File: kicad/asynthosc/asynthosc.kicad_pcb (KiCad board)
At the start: 4 copper layers, 69 x 106 mm, 210 parts, among them J1 USB_B_Micro, J10 AudioJack3, J11 AudioJack3, J12 RJ45_LED_Shielded, J13 AudioJack3, J14 AudioJack3, J2 Conn_02x05_Odd_Even, J3 Conn_ARM_SWD_TagConnect_TC203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, J4 Conn_02x07_Odd_Even, J5 Conn_02x04_Odd_Even, J6 AudioJack3, J7 AudioJack3, J8 AudioJack3, J9 AudioJack3, Q1 Q_NPN_BEC, Q2 Q_NPN_BEC, SW1 SW_Push, SW2 SW_MEC_5G_LED, SW3 SW_DIP_x02, SW4 SW_DIP_x02, SW5 SW_MEC_5G_LED, SW6 RotaryEncoder, SW7 SW_MEC_5G_LED, SW8 SW_MEC_5G_LED, U1 LM1117S-3.3, U10 LAN8742A, U11 USBLC6-2P6, U12 H11L1, U13 USBLC6-2P6, U2 LMR62421XMF, U3 USBLC6-2SC6, U4 LM1117S-5.0, U5 Si1869DH, U6 STM32F723VETx, U7 W25Q32JVSS, U8 MCP6004, U9 MCP6004, Y1 8MHz, 8pF, Y2 25MHZ,20PF,30PPM

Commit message: pcb: routing
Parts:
- moved SW1 5.54 mm to (101.8, 108.2)
- moved D22 4.98 mm to (89.8, 111.8)
- moved R69 0.50 mm to (130.8, 124.8)
- turned R32 to 0 degrees
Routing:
- net 5V: track 160.1 -> 141.3 mm
- net GND: track 42.5 -> 57.5 mm, vias 214 -> 316
- net /Soc/NRST: track 31.6 -> 39.5 mm
- net Net-(U8A--): track 0.00 -> 7.10 mm
- net /Soc/JTCK_CONN: track 61.7 -> 56.5 mm
- net /Analog_in/CVIN1: track 69.1 -> 65.0 mm
- net Net-(SW3B-2): track 1.49 -> 3.69 mm
- net Net-(SW3A-2): track 0.00 -> 2.19 mm
- net Net-(J6-PadT): track 37.4 -> 39.3 mm
- net 3V3_FILT: track 9.46 -> 8.76 mm, vias 9 -> 11
- net /Soc/Ethernet/TX_P: track 25.3 -> 24.7 mm
- net /Soc/Ethernet/TX_N: track 26.6 -> 26.0 mm
- net /Analog_in/CVIN0: track 70.5 -> 71.0 mm
- net 3V3: vias 19 -> 48

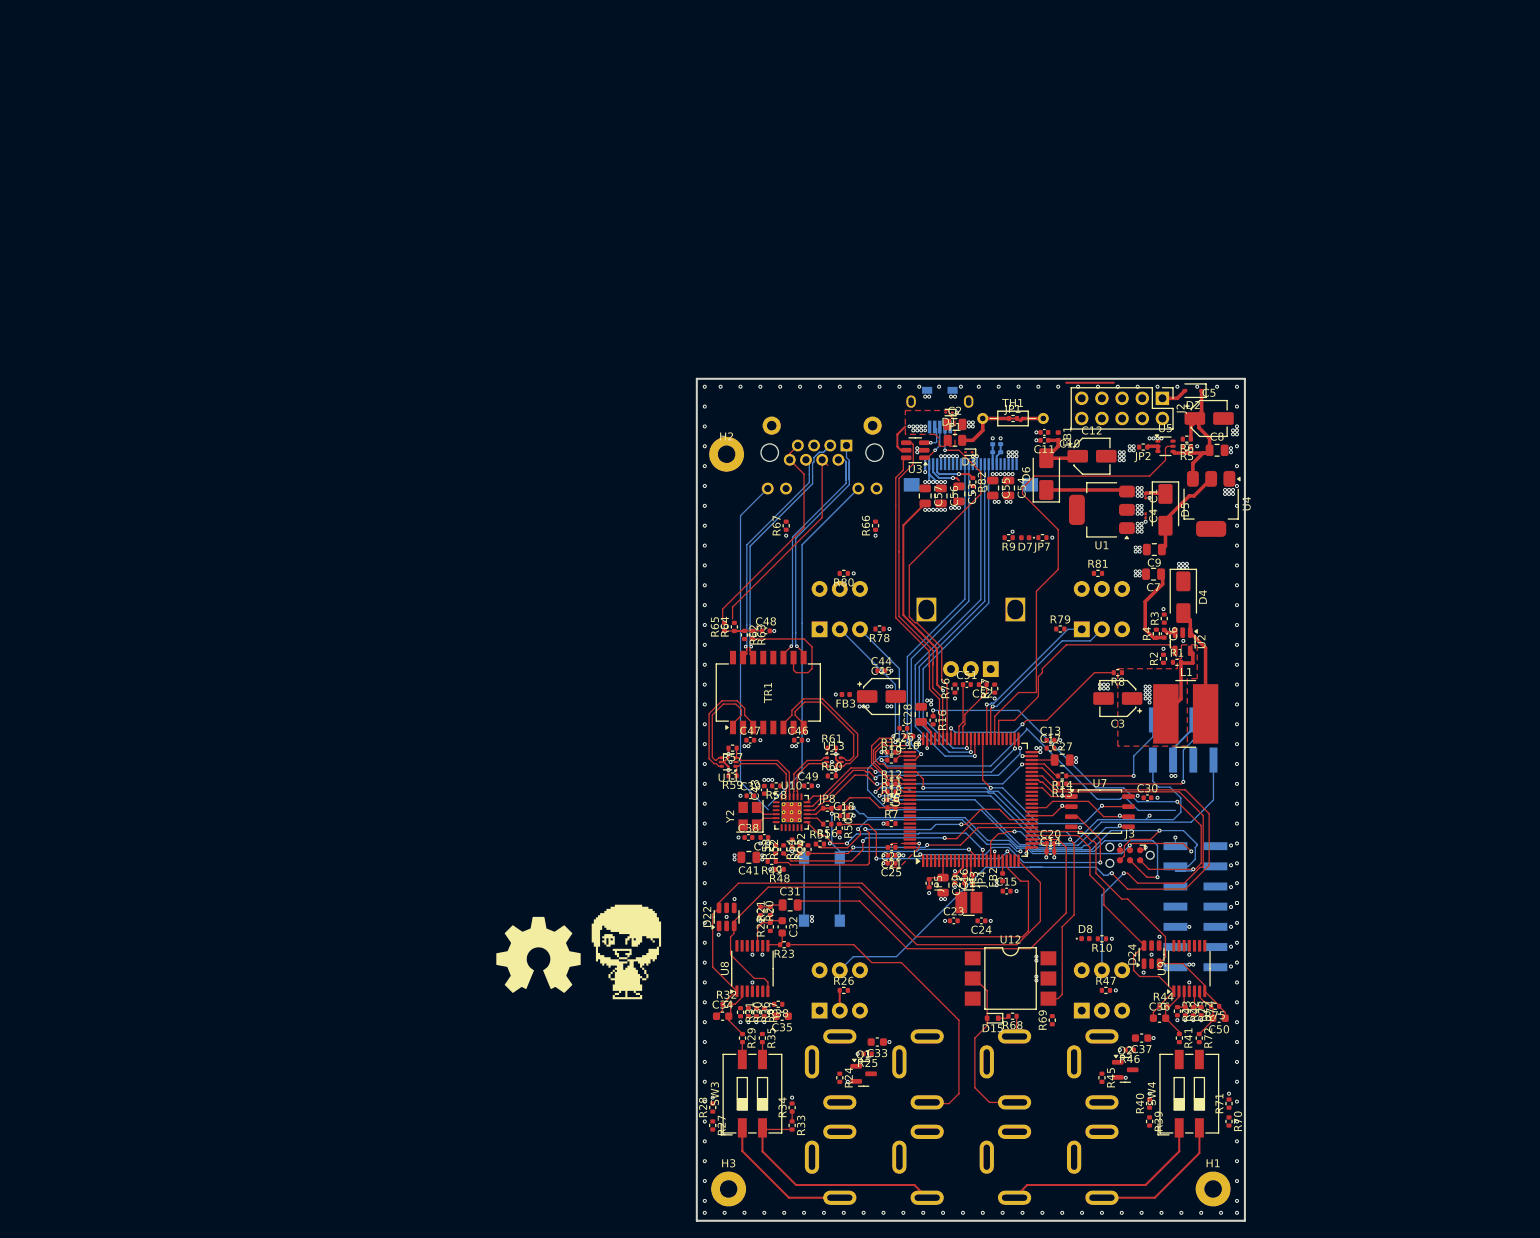
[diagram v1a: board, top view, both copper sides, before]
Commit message: sch: pcb: fix pin errors
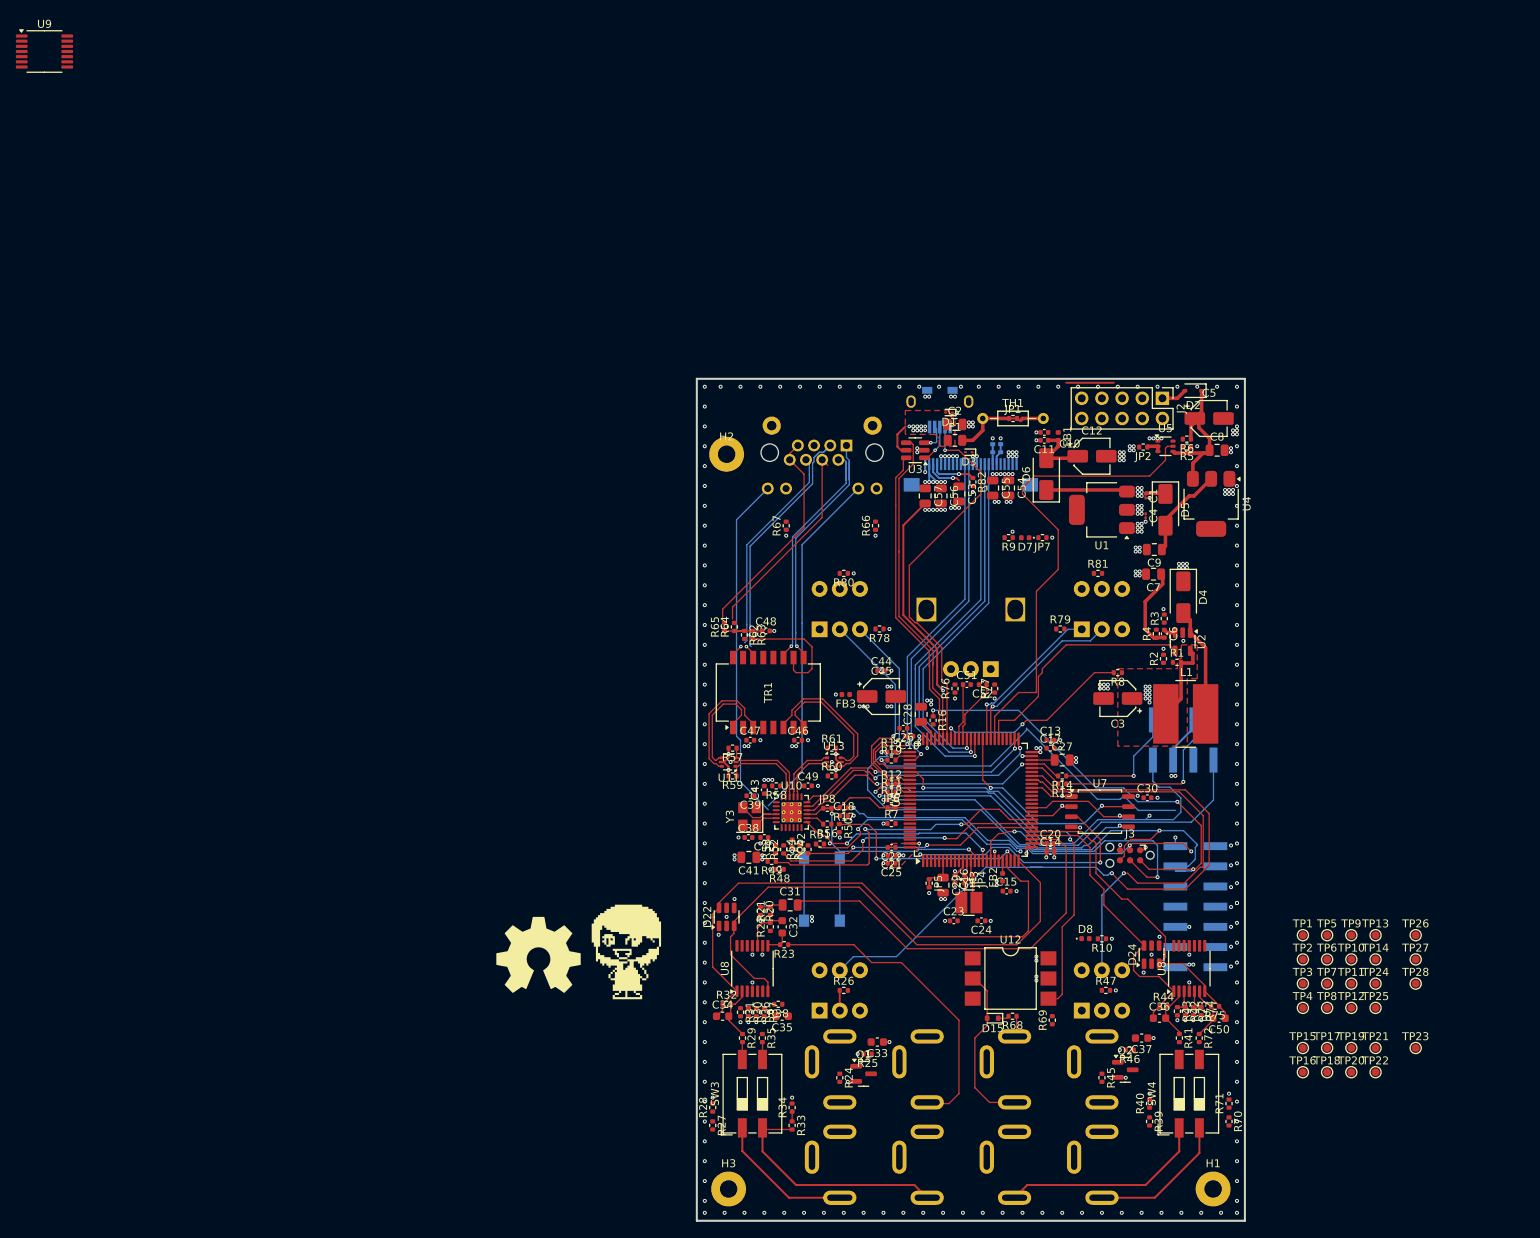
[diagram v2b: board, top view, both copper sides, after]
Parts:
- removed Y2: 25MHZ,20PF,30PPM, Crystal:Crystal_SMD_3225-4Pin_3.2x2.5mm
- added TP1: TestPoint, TestPoint:TestPoint_Pad_D1.0mm, F.Cu at (162.3, 114.0)
- added TP10: TestPoint, TestPoint:TestPoint_Pad_D1.0mm, F.Cu at (168.4, 117.1)
- added TP11: TestPoint, TestPoint:TestPoint_Pad_D1.0mm, F.Cu at (168.4, 120.2)
- added TP12: TestPoint, TestPoint:TestPoint_Pad_D1.0mm, F.Cu at (168.4, 123.2)
- added TP13: TestPoint, TestPoint:TestPoint_Pad_D1.0mm, F.Cu at (171.4, 114.0)
- added TP14: TestPoint, TestPoint:TestPoint_Pad_D1.0mm, F.Cu at (171.4, 117.1)
- added TP15: TestPoint, TestPoint:TestPoint_Pad_D1.0mm, F.Cu at (162.3, 128.2)
- added TP16: TestPoint, TestPoint:TestPoint_Pad_D1.0mm, F.Cu at (162.3, 131.3)
- added TP17: TestPoint, TestPoint:TestPoint_Pad_D1.0mm, F.Cu at (165.3, 128.2)
- added TP18: TestPoint, TestPoint:TestPoint_Pad_D1.0mm, F.Cu at (165.3, 131.3)
- added TP19: TestPoint, TestPoint:TestPoint_Pad_D1.0mm, F.Cu at (168.4, 128.2)
- added TP2: TestPoint, TestPoint:TestPoint_Pad_D1.0mm, F.Cu at (162.3, 117.1)
- added TP20: TestPoint, TestPoint:TestPoint_Pad_D1.0mm, F.Cu at (168.4, 131.3)
- added TP21: TestPoint, TestPoint:TestPoint_Pad_D1.0mm, F.Cu at (171.4, 128.2)
- added TP22: TestPoint, TestPoint:TestPoint_Pad_D1.0mm, F.Cu at (171.4, 131.3)
- added TP23: TestPoint, TestPoint:TestPoint_Pad_D1.0mm, F.Cu at (176.5, 128.2)
- added TP24: TestPoint, TestPoint:TestPoint_Pad_D1.0mm, F.Cu at (171.4, 120.2)
- added TP25: TestPoint, TestPoint:TestPoint_Pad_D1.0mm, F.Cu at (171.4, 123.2)
- added TP26: TestPoint, TestPoint:TestPoint_Pad_D1.0mm, F.Cu at (176.5, 114.0)
- added TP27: TestPoint, TestPoint:TestPoint_Pad_D1.0mm, F.Cu at (176.5, 117.1)
- added TP28: TestPoint, TestPoint:TestPoint_Pad_D1.0mm, F.Cu at (176.5, 120.2)
- added TP3: TestPoint, TestPoint:TestPoint_Pad_D1.0mm, F.Cu at (162.3, 120.2)
- added TP4: TestPoint, TestPoint:TestPoint_Pad_D1.0mm, F.Cu at (162.3, 123.2)
- added TP5: TestPoint, TestPoint:TestPoint_Pad_D1.0mm, F.Cu at (165.3, 114.0)
- added TP6: TestPoint, TestPoint:TestPoint_Pad_D1.0mm, F.Cu at (165.3, 117.1)
- added TP7: TestPoint, TestPoint:TestPoint_Pad_D1.0mm, F.Cu at (165.3, 120.2)
- added TP8: TestPoint, TestPoint:TestPoint_Pad_D1.0mm, F.Cu at (165.3, 123.2)
- added TP9: TestPoint, TestPoint:TestPoint_Pad_D1.0mm, F.Cu at (168.4, 114.0)
- added U9: MCP6004, Package_SO:TSSOP-14_4.4x5mm_P0.65mm, F.Cu at (3.88, 2.80)
- added Y3: 25MHZ,20PF,30PPM, Crystal:Crystal_SMD_3225-4Pin_3.2x2.5mm, F.Cu at (92.7, 99.1)
- turned C39 to 180 degrees
- renumbered U9 to U8
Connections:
- R62 pad 2: /Soc/Ethernet/RJ_RX_N -> Net-(TR1-C_TX)
- TR1 pad 15: /Soc/Ethernet/RJ_RX_N -> Net-(TR1-C_TX)
- TR1 pad 16: unconnected-(TR1-TX+-Pad16) -> /Soc/Ethernet/RJ_RX_N
- U8 pad 12: (no net) -> unconnected-(U8D-+-Pad12) (x2)
- U8 pad 13: (no net) -> unconnected-(U8D---Pad13) (x2)
- U8 pad 14: (no net) -> unconnected-(U8-Pad14) (x2)
- U8 pad 1: /Analog_in/CVIN2 -> /Analog_in/CVIN0
- U8 pad 10: (no net) -> Net-(U8C-+)
- U8 pad 2: Net-(U9A--) -> Net-(U8A--)
- U8 pad 3: Net-(U9A-+) -> Net-(U8A-+)
- U8 pad 5: Net-(U9B-+) -> Net-(U8B-+)
- U8 pad 6: Net-(U9B--) -> Net-(U8B--)
- U8 pad 7: /Analog_in/CVIN3 -> /Analog_in/CVIN1
- U8 pad 8: (no net) -> Net-(C32-Pad2)
- U8 pad 9: (no net) -> GND
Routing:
- net Net-(U10-XTAL2): track 2.81 -> 5.76 mm

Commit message: sch: pcb: tiny fixes and changes
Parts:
- added C58: 2.2u X7R, Capacitor_SMD:C_0402_1005Metric, F.Cu at (70.3, 101.0)
- added J15: Conn_02x04_Odd_Even, Connector_PinHeader_2.54mm:PinHeader_2x04_P2.54mm_Vertical_SMD, F.Cu at (178.1, 105.8)
- added R83: 3k, Resistor_SMD:R_0402_1005Metric, F.Cu at (70.7, 101.0)
- added TP29: TestPoint, TestPoint:TestPoint_Pad_D1.0mm, F.Cu at (188.0, 101.2)
- added TP30: TestPoint, TestPoint:TestPoint_Pad_D1.0mm, F.Cu at (188.0, 104.2)
- moved R10 12.9 mm to (125.0, 109.7), turned to 0 degrees
- moved D8 10.5 mm to (125.0, 111.0)
- moved TP1 1.00 mm to (163.3, 114.0)
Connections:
- U6 pad 17: unconnected-(U6-PC2-Pad17) -> /Soc/DBG_LED
- U6 pad 53: unconnected-(U6-REXTPHYHS-Pad53) -> /Soc/OTGHS_EXTR
- U6 pad 55: unconnected-(U6-V12PHYHS-Pad55) -> /Soc/OTGHS_VDD12
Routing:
- net 3V3: track 65.1 -> 120.9 mm, vias 48 -> 47
- net +10V: track 69.7 -> 13.9 mm
- net /Soc/DBG_LED: track 0.00 -> 7.16 mm
- net Net-(D8-A): track 0.00 -> 1.31 mm
- net Net-(J5-Pin_7): track 54.6 -> 53.9 mm, vias 2 -> 1

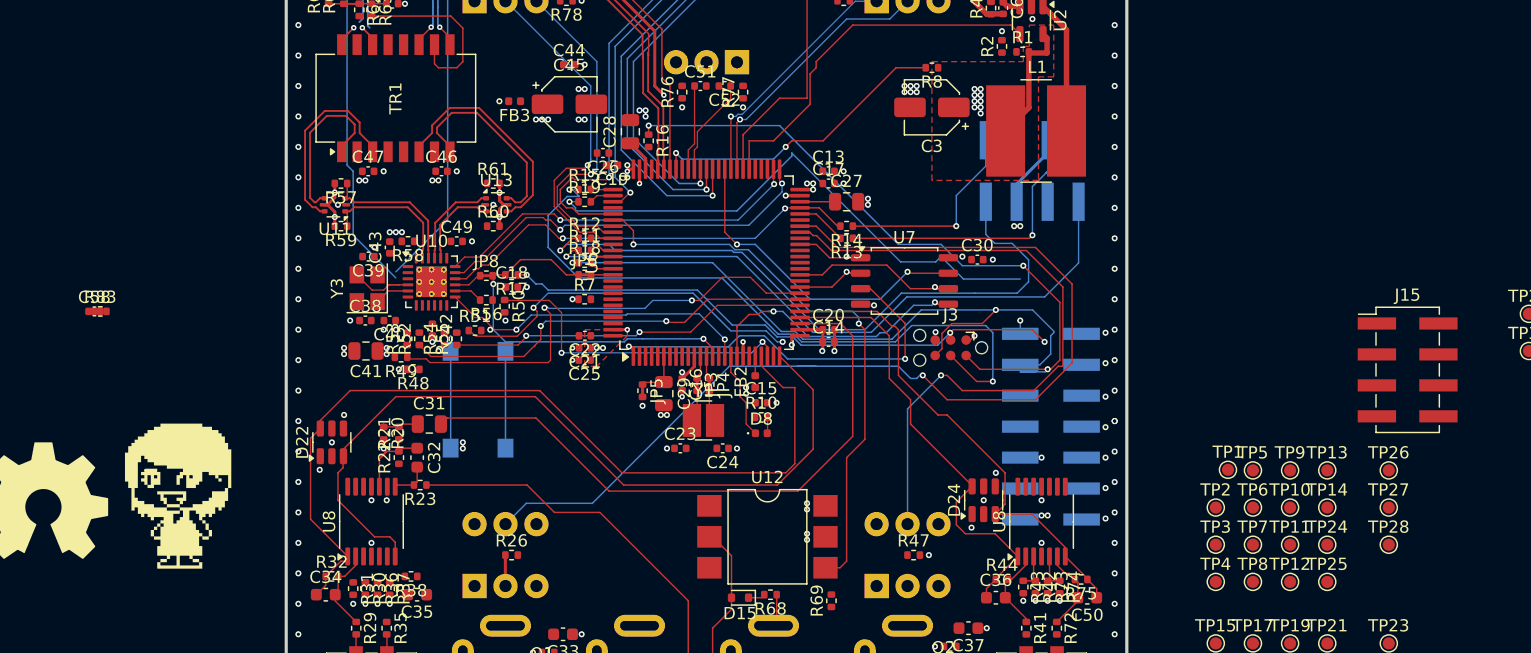
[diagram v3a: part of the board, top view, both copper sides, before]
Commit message: sch: pcb: add gpio output connector for optional LEDs on decorative board
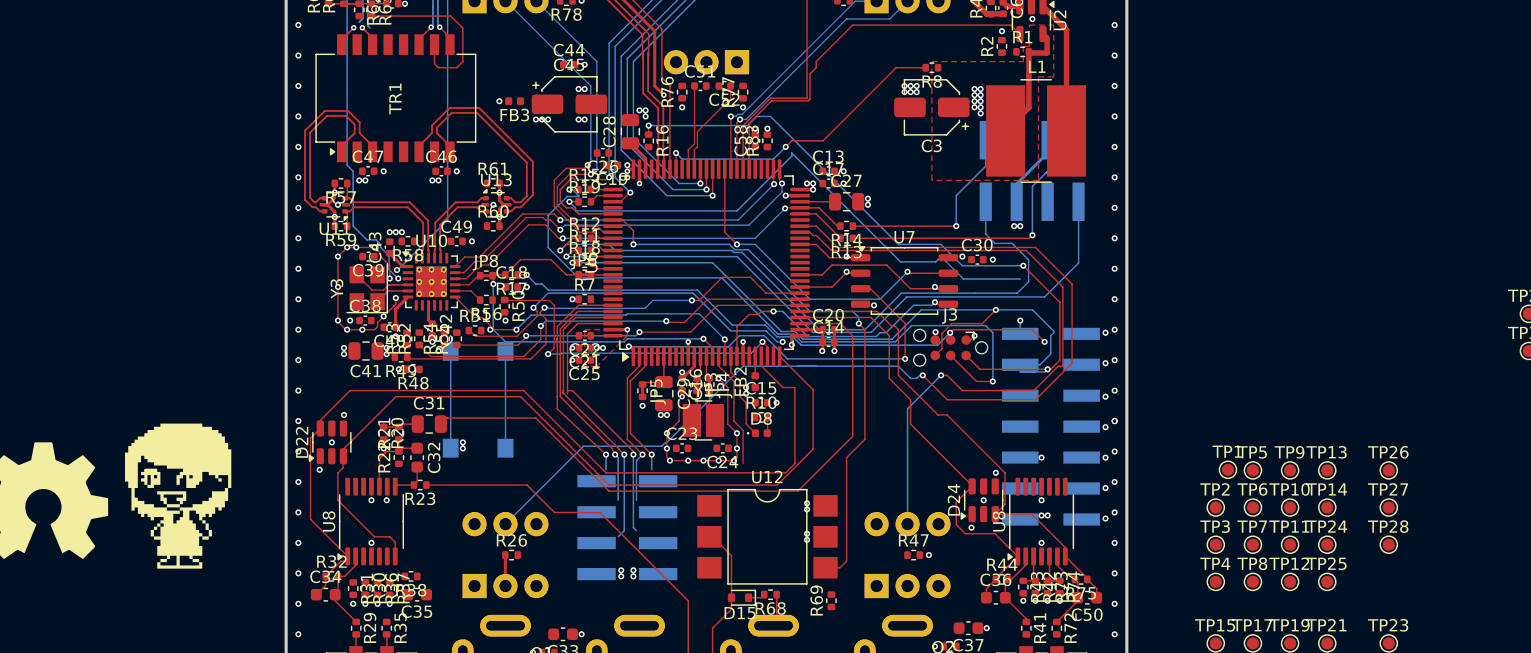
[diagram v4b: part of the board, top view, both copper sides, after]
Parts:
- J15: moved to B.Cu
- moved J15 65.3 mm to (114.0, 118.8), turned to 180 degrees
- moved R83 56.5 mm to (125.5, 87.0), turned to 90 degrees
- moved C58 56.0 mm to (124.5, 87.0), turned to 90 degrees
- moved C40 0.55 mm to (94.5, 102.3)
- moved C23 0.15 mm to (118.5, 112.2)
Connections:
- J15 pad 1: unconnected-(J15-Pin_1-Pad1) -> /Soc/EXT_LED1
- J15 pad 2: unconnected-(J15-Pin_2-Pad2) -> /Soc/EXT_LED2
- J15 pad 3: unconnected-(J15-Pin_3-Pad3) -> /Soc/EXT_LED3
- J15 pad 4: unconnected-(J15-Pin_4-Pad4) -> /Soc/EXT_LED4
- J15 pad 5: unconnected-(J15-Pin_5-Pad5) -> /Soc/EXT_LED5
- J15 pad 6: unconnected-(J15-Pin_6-Pad6) -> /Soc/EXT_LED6
- J15 pad 7: unconnected-(J15-Pin_7-Pad7) -> 3V3
- J15 pad 8: unconnected-(J15-Pin_8-Pad8) -> GND
- U6 pad 2: unconnected-(U6-PE3-Pad2) -> /Soc/EXT_LED3
- U6 pad 3: unconnected-(U6-PE4-Pad3) -> /Soc/EXT_LED1
- U6 pad 35: /Soc/ADC1_IN8 -> /Soc/EXT_LED1
- U6 pad 95: unconnected-(U6-PB8-Pad95) -> /Soc/EXT_LED2
- U6 pad 96: unconnected-(U6-PB9-Pad96) -> /Soc/EXT_LED4
- U6 pad 97: unconnected-(U6-PE0-Pad97) -> /Soc/EXT_LED6
- U6 pad 98: unconnected-(U6-PE1-Pad98) -> /Soc/EXT_LED5
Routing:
- net +10V: track 13.9 -> 69.7 mm
- net 3V3: track 120.9 -> 69.6 mm, vias 47 -> 49
- net GND: track 57.5 -> 95.7 mm, vias 316 -> 338
- net /Soc/EXT_LED6: track 0.00 -> 24.0 mm, vias 0 -> 1
- net /Soc/EXT_LED5: track 0.00 -> 23.1 mm, vias 0 -> 1
- net /Soc/EXT_LED4: track 0.00 -> 20.9 mm, vias 0 -> 1
- net /Soc/EXT_LED2: track 0.00 -> 19.1 mm, vias 0 -> 1
- net /Soc/EXT_LED3: track 0.00 -> 13.0 mm, vias 0 -> 1
- net /Soc/EXT_LED1: track 0.00 -> 10.6 mm, vias 0 -> 1
- net /Soc/ADC1_IN9: track 0.00 -> 9.65 mm
- net 3V3_FILT: track 8.76 -> 10.7 mm
- net /Soc/RMII_RXD1: track 39.2 -> 38.0 mm
- net /Soc/RMII_REF_CLK: track 26.9 -> 28.1 mm
- net /Soc/Ethernet/RJ45_LED1: track 43.9 -> 44.7 mm, vias 0 -> 1
- net /Soc/JTMS_CONN: track 57.4 -> 58.0 mm
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
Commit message: sch: pcb: wip and silkscreen cleaning
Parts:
- removed TP1, TP10, TP11, TP12, TP13, TP14, TP15, TP16, TP17, TP18, TP19, TP2, TP20, TP21, TP22, TP23, TP24, TP25, TP26, TP27, TP28, TP29, TP3, TP30, TP4, TP5, TP6, TP7, TP8, TP9: TestPoint, TestPoint:TestPoint_Pad_D1.0mm
- removed the U8 at (148.0, 118.2)
- added JP11: SolderJumper_2_Bridged, asynthosc:SolderJumper_0402_1005Metric_Bridged, F.Cu at (125.5, 87.0)
- moved U9 184.7 mm to (148.0, 118.2), turned to 90 degrees
- moved J4 4.78 mm to (144.0, 110.8), turned to -90 degrees
- moved R83 1.00 mm to (126.5, 87.0)
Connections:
- net /Soc/NRST renamed /Soc/nRST
- U6 pad 39: /Soc/TIM1_CH1 -> unconnected-(U6-PE9-Pad39)
- U6 pad 4: /Soc/TIM15_CH1 -> unconnected-(U6-PE5-Pad4)
- U6 pad 5: /Soc/TIM15_CH2 -> unconnected-(U6-PE6-Pad5)
- U6 pad 54: unconnected-(U6-VDDPHYHS-Pad54) -> Net-(JP11-A)
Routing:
- net /Soc/JTCK_CONN: track 56.5 -> 78.9 mm
- net /Soc/JTDI_CONN: track 46.0 -> 64.2 mm, vias 2 -> 1
- net Net-(J5-Pin_1): track 53.2 -> 47.3 mm, vias 1 -> 2
- net Net-(J5-Pin_7): track 53.9 -> 49.0 mm, vias 1 -> 2
- net /Soc/NRST_CONN: track 46.6 -> 48.6 mm, vias 3 -> 2
- net Net-(U9D--): track 0.00 -> 1.39 mm, vias 0 -> 1
- net /Soc/nRST: track 39.5 -> 40.8 mm
- net Net-(U9D-+): track 0.00 -> 1.15 mm, vias 0 -> 1
- net Net-(TP28-Pad1): track 0.00 -> 1.13 mm, vias 0 -> 1
- net /Analog_in/TRG0: track 54.7 -> 55.7 mm
- net /Soc/JTDO_CONN: track 56.4 -> 57.2 mm
- net GND: vias 338 -> 331
- net 3V3: vias 49 -> 50
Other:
- board text added: "3V3"
- board text added: "Asynth2Osc V0.1"
- board text added: "CANCEL"
- board text added: "GND"
- board text added: "JTCK"
- board text added: "JTDI"
- board text added: "JTDO"
- board text added: "JTMS"
- board text added: "NRST"
- board text added: "OK"
- board text added: "RESET"
- board text added: "RX2"
- board text added: "RX3"
- board text added: "RederoTech 2024"
- board text added: "TRG0"
- board text added: "TRG1"
- board text added: "TX2"
- board text added: "TX3"
